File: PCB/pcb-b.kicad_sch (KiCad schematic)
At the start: 23 parts, among them Q13 TPCA8120,L1Q, Q9 BC817, U1 L7805, U2 L7805, U3 L7805

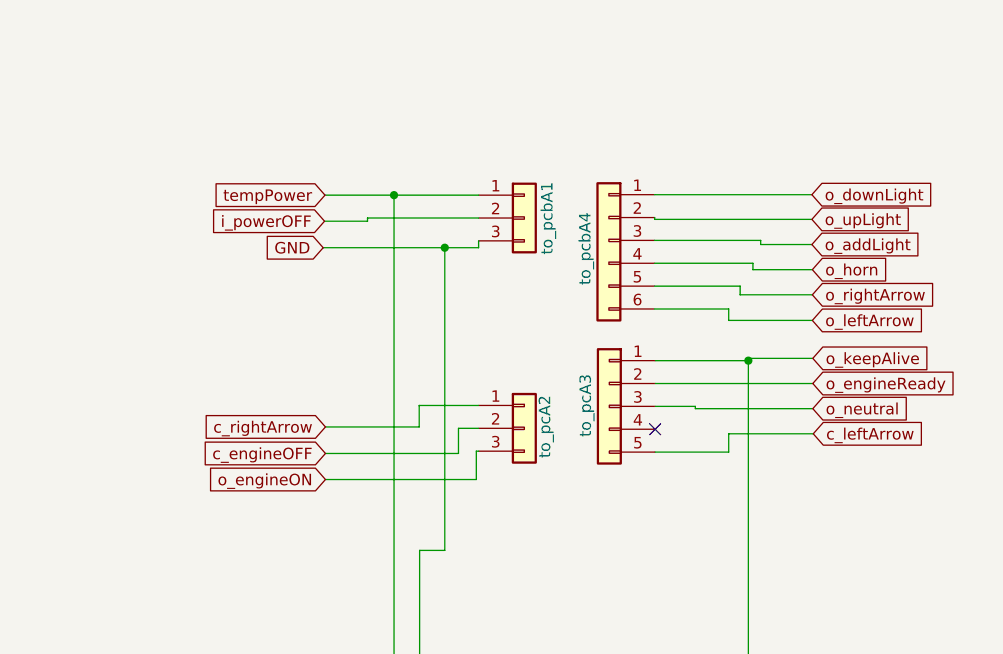
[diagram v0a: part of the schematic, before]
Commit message: Pin-header connectors adjustment
The main idea to mount the two pcb-A on the pcbB has been dropped, because the result is a too much chatic one and I realized that
wires welder on the top is a dangerous solution, they can create unwanted contacts and short-circuits... So, I choise to place the
two PCB beside. So, in order to get a more ordered and clean solution, I am using flat cables instead wires, and pin-header
connectors instead of welding them directly. I foung good connectors where every female-plug is blocked in its male-socket. But,
they are available just for even numbers of pins. For this reason, I have adjusted all the pin-header connectors and their
positions.
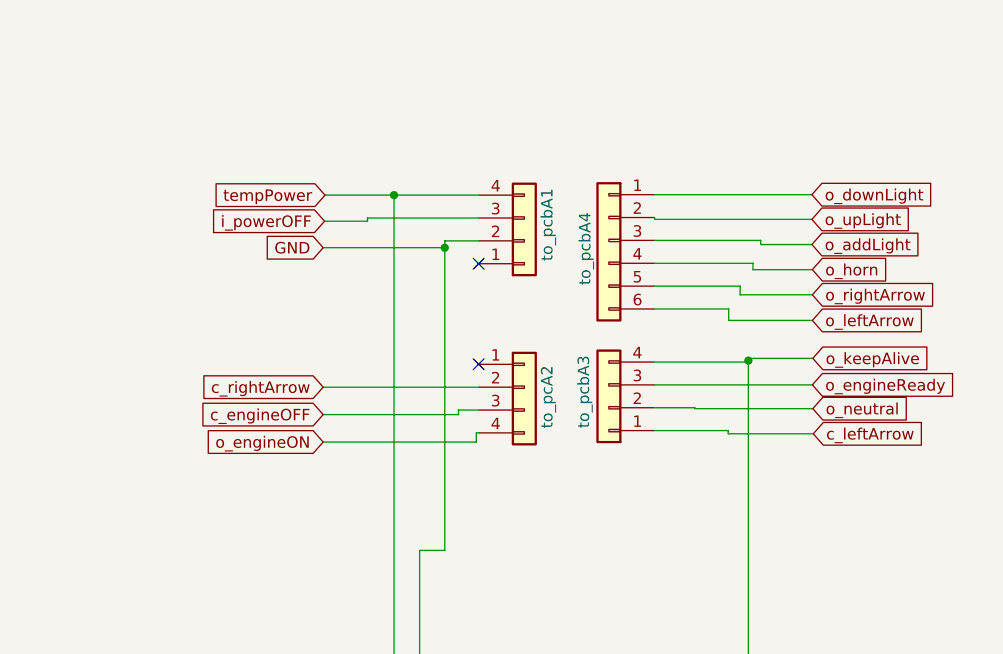
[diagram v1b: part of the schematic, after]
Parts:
- removed to_pcA2, to_pcbA1: Conn_01x03, Connector_PinSocket_2.54mm:PinSocket_1x03_P2.54mm_Vertical, symbol Connector_Generic:Conn_01x03
- removed to_pcA3: Conn_01x05, Connector_PinSocket_2.54mm:PinSocket_1x05_P2.54mm_Vertical, symbol Connector_Generic:Conn_01x05
- added to_pcA2, to_pcbA1, to_pcbA3: Conn_01x04, Connector_PinSocket_2.54mm:PinSocket_1x04_P2.54mm_Vertical, symbol Connector_Generic:Conn_01x04
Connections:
- net GND: now also to_pcbA1.2 (Pin_2)
- net c_engineOFF: now also to_pcA2.3 (Pin_3)
- net c_leftArrow: now also to_pcbA3.1 (Pin_1)
- net c_rightArrow: now also to_pcA2.2 (Pin_2)
- net i_powerOFF: now also to_pcbA1.3 (Pin_3)
- net o_engineON: now also to_pcA2.4 (Pin_4)
- net o_engineReady: now also to_pcbA3.3 (Pin_3)
- net o_keepAlive: now also to_pcbA3.4 (Pin_4)
- net o_neutral: now also to_pcbA3.2 (Pin_2)
- net tempPower: now also to_pcbA1.4 (Pin_4)
- no-connect marks 1 -> 2

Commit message: Important fixes and adjustments
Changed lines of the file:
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@@
-	)
-	(symbol
-		(lib_id "power:PWR_FLAG")
-		(at 140.97 159.512 180)
-		(unit 1)
-		(exclude_from_sim no)
-		(in_bom yes)
-		(on_board yes)
-		(dnp no)
-		(property "Reference" "#FLG0101"
-			(at 140.97 161.417 0)
-			(effects
-				(font
-					(size 1.27 1.27)
-				)
-				(hide yes)
-			)
-		)
-		(property "Value" "PWR_FLAG"
-			(at 140.97 163.576 0)
-			(effects
-				(font
-					(size 1.27 1.27)
-				)
-			)
-		)
-		(property "Footprint" ""
-			(at 140.97 159.512 0)
-			(effects
-				(font
-					(size 1.27 1.27)
-				)
-				(hide yes)
-			)
-		)
-		(property "Datasheet" "~"
-			(at 140.97 159.512 0)
-			(effects
-				(font
-					(size 1.27 1.27)
-				)
-				(hide yes)
-			)
-		)
-		(property "Description" ""
-			(at 140.97 159.512 0)
-			(effects
-				(font
-					(size 1.27 1.27)
-				)
-				(hide yes)
-			)
-		)
-		(pin "1"
-		)
-		(instances
-			(project "pcb-b"
-				(path "/709d0967-afe5-49d3-92a5-d2bb94550bdb"
-					(reference "#FLG0101")
-					(unit 1)
-				)
-			)
-		)
 	)
 	(symbol

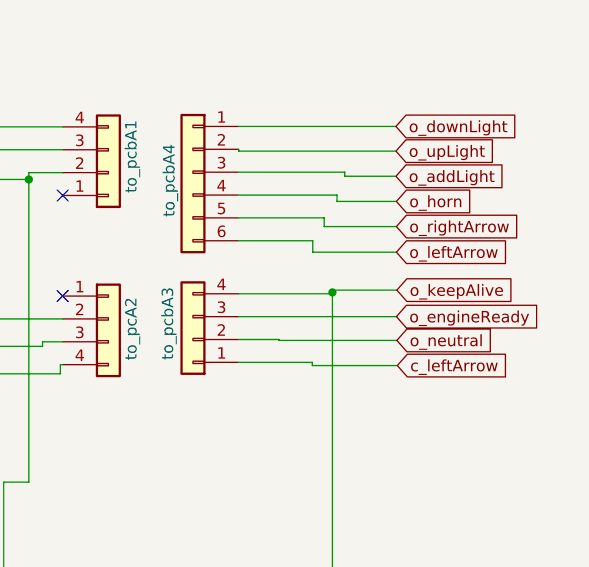
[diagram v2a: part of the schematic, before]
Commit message: o_NEUTRAL is connected directly to the led
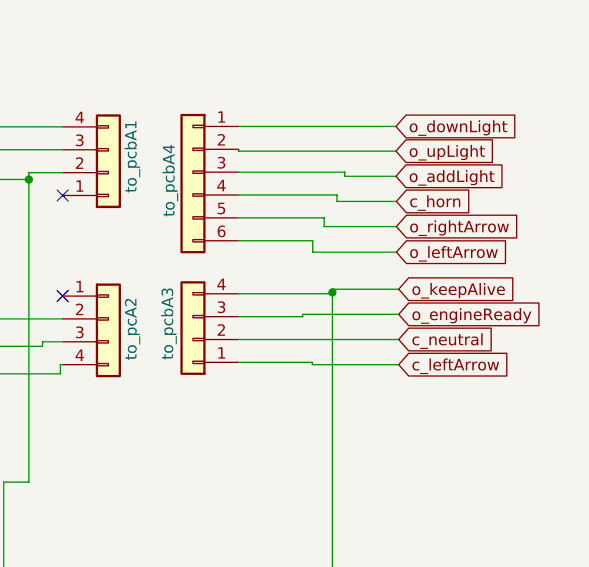
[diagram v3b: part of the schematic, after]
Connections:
- net o_horn renamed c_horn
- net o_neutral renamed c_neutral
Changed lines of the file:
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@@
 	(wire
 		(pts
-			(xy 174.3964 103.124) (xy 169.926 103.124)
-		)
-		(stroke
-			(width 0)
-			(type default)
-		)
-	)
-	(wire
-		(pts
-			(xy 187.5536 106.0196) (xy 178.1048 106.0196)
+			(xy 169.926 103.124) (xy 187.706 103.124)
+		)
+		(stroke
+			(width 0)
+			(type default)
+		)
+	)
+	(wire
+		(pts
+			(xy 177.038 100.33) (xy 187.706 100.33)
+		)
+		(stroke
+			(width 0)
+			(type default)
+		)
+	)
+	(wire
+		(pts
+			(xy 187.706 105.918) (xy 178.1048 105.918)
 		)
 		(stroke
@@
 	(wire
 		(pts
-			(xy 178.1048 106.0196) (xy 178.1048 105.664)
+			(xy 178.1048 105.918) (xy 178.1048 105.664)
 		)
 		(stroke
@@
 	(wire
 		(pts
-			(xy 187.5028 103.2256) (xy 174.3964 103.2256)
-		)
-		(stroke
-			(width 0)
-			(type default)
-		)
-	)
-	(wire
-		(pts
 			(xy 45.72 169.3164) (xy 45.72 171.8564)
 		)
@@
 	(wire
 		(pts
-			(xy 180.34 97.6376) (xy 187.5028 97.6376)
+			(xy 180.34 97.536) (xy 187.706 97.536)
 		)
 		(stroke
@@
 	(wire
 		(pts
+			(xy 177.038 100.584) (xy 169.926 100.584)
+		)
+		(stroke
+			(width 0)
+			(type default)
+		)
+	)
+	(wire
+		(pts
 			(xy 64.9732 114.554) (xy 55.2196 114.554)
 		)
@@
 	(wire
 		(pts
-			(xy 169.926 100.584) (xy 187.5028 100.584)
-		)
-		(stroke
-			(width 0)
-			(type default)
-		)
-	)
-	(wire
-		(pts
 			(xy 135.7122 150.0632) (xy 135.6868 161.544)
 		)
@@
 	(wire
 		(pts
-			(xy 174.3964 103.2256) (xy 174.3964 103.124)
-		)
-		(stroke
-			(width 0)
-			(type default)
-		)
-	)
-	(wire
-		(pts
 			(xy 146.6088 85.344) (xy 146.6088 118.9736)
 		)
@@
 	(wire
 		(pts
+			(xy 177.038 100.33) (xy 177.038 100.584)
+		)
+		(stroke
+			(width 0)
+			(type default)
+		)
+	)
+	(wire
+		(pts
 			(xy 63.4492 158.75) (xy 63.5 158.75)
 		)
@@
 	(wire
 		(pts
-			(xy 180.34 97.8916) (xy 180.34 97.6376)
+			(xy 180.34 97.8916) (xy 180.34 97.536)
 		)
 		(stroke
@@
 		)
 	)
-	(global_label "o_horn"
+	(global_label "c_horn"
 		(shape input)
 		(at 187.452 87.7824 0)
@@
 		)
 		(property "Intersheetrefs" "${INTERSHEET_REFS}"
-			(at 187.452 87.7824 0)
-			(effects
-				(font
-					(size 1.27 1.27)
-				)
+			(at 196.7266 87.7824 0)
+			(effects
+				(font
+					(size 1.27 1.27)
+				)
+				(justify left)
 				(hide yes)
 			)
 		)
 		(property "Riferimenti inter-foglio" "${INTERSHEET_REFS}"
-			(at 196.2151 87.703 0)
+			(at 187.452 89.9732 0)
 			(effects
 				(font
@@
 	(global_label "o_keepAlive"
 		(shape input)
-		(at 187.5028 97.6376 0)
+		(at 187.706 97.536 0)
 		(fields_autoplaced yes)
 		(effects
@@
 		)
 		(property "Intersheetrefs" "${INTERSHEET_REFS}"
-			(at 187.5028 97.6376 0)
+			(at 187.706 97.536 0)
 			(effects
 				(font
@@
 		)
 		(property "Riferimenti inter-foglio" "${INTERSHEET_REFS}"
-			(at 200.8016 97.5582 0)
+			(at 201.0048 97.4566 0)
 			(effects
 				(font
@@
 	(global_label "c_leftArrow"
 		(shape input)
-		(at 187.5536 106.0196 0)
+		(at 187.706 105.918 0)
 		(fields_autoplaced yes)
 		(effects
@@
 		)
 		(property "Intersheetrefs" "${INTERSHEET_REFS}"
-			(at 187.5536 106.0196 0)
+			(at 187.706 105.918 0)
 			(effects
 				(font
@@
 		)
 		(property "Riferimenti inter-foglio" "${INTERSHEET_REFS}"
-			(at 200.3686 105.9402 0)
+			(at 200.521 105.8386 0)
 			(effects
 				(font
@@
 	(global_label "o_engineReady"
 		(shape input)
-		(at 187.452 100.584 0)
+		(at 187.706 100.33 0)
 		(fields_autoplaced yes)
 		(effects
@@
 		)
 		(property "Intersheetrefs" "${INTERSHEET_REFS}"
-			(at 187.452 100.584 0)
+			(at 187.706 100.33 0)
 			(effects
 				(font
@@
 		)
 		(property "Riferimenti inter-foglio" "${INTERSHEET_REFS}"
-			(at 203.8351 100.5046 0)
+			(at 204.0891 100.2506 0)
 			(effects
 				(font
@@
 		)
 	)
-	(global_label "o_neutral"
+	(global_label "c_neutral"
 		(shape input)
-		(at 187.5028 103.2256 0)
+		(at 187.706 103.124 0)
 		(fields_autoplaced yes)
 		(effects
@@
 		)
 		(property "Intersheetrefs" "${INTERSHEET_REFS}"
-			(at 187.5028 103.2256 0)
-			(effects
-				(font
-					(size 1.27 1.27)
-				)
+			(at 199.4601 103.124 0)
+			(effects
+				(font
+					(size 1.27 1.27)
+				)
+				(justify left)
 				(hide yes)
 			)
 		)
 		(property "Riferimenti inter-foglio" "${INTERSHEET_REFS}"
-			(at 198.7454 103.1462 0)
-			(effects
-				(font
+			(at 187.706 105.3148 0)
+			(effects
+				(font

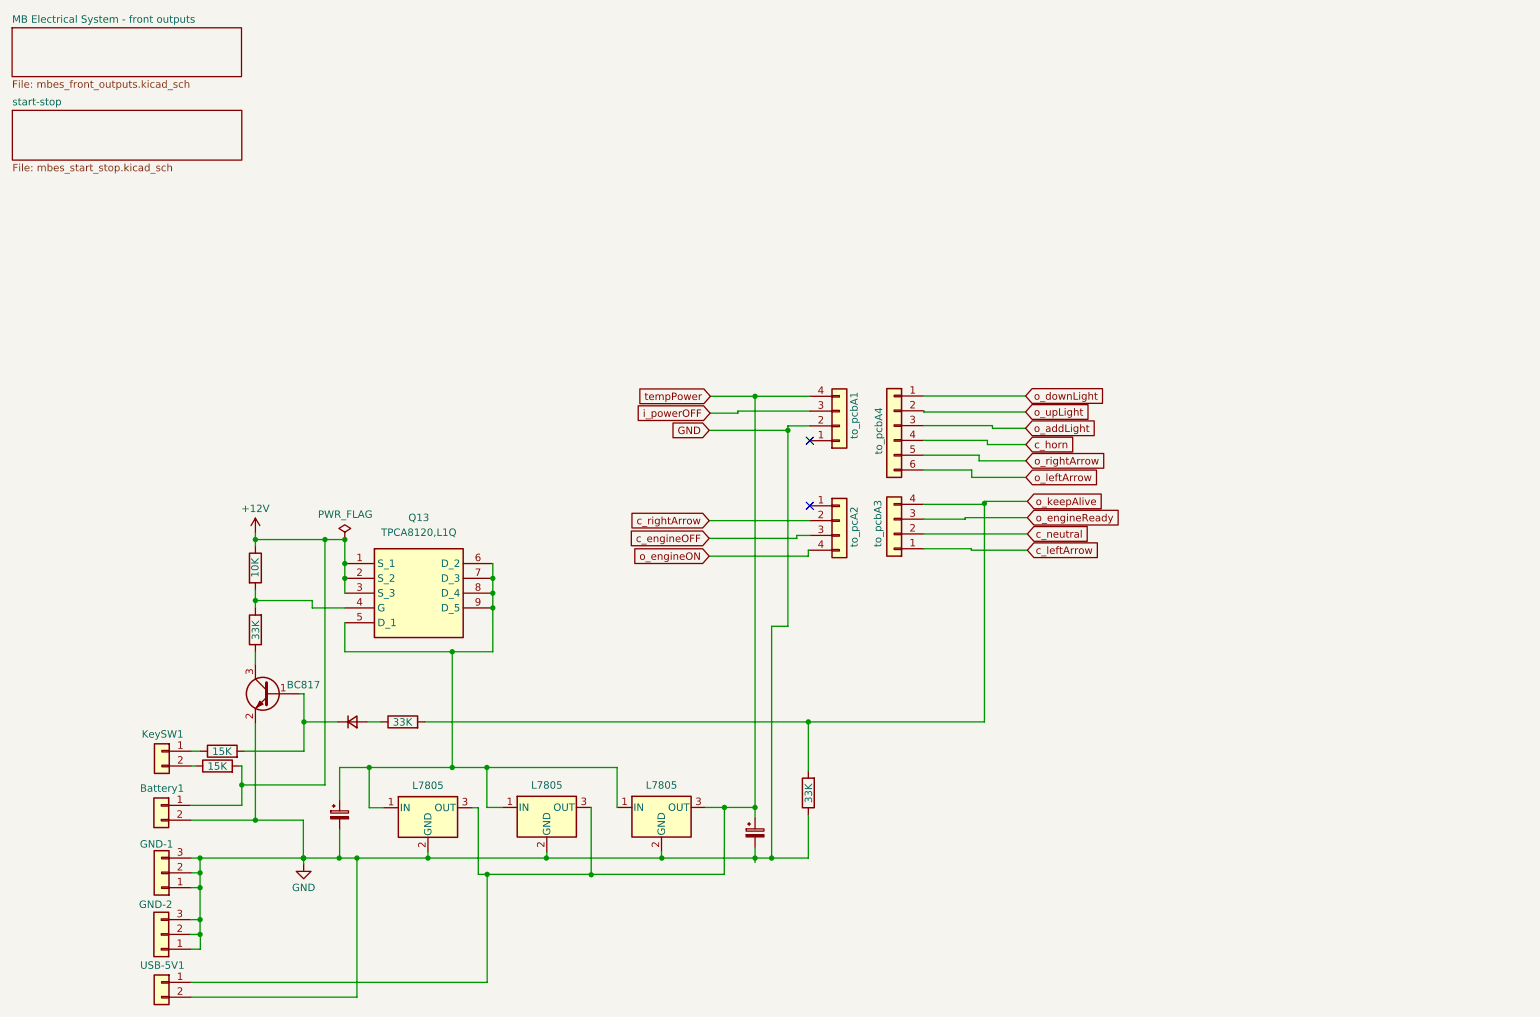
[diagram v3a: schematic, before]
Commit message: No USB support and PCB-B size reducing
Implementing USB power support using 7805 was a stupid idea: too much wasted electic current in Joule effect. So, I moved just
one 7805 in the PCB-A, because the its used power is very low. It allowed me to optimize the PCB-B used space and reduce its
whole size ;-)
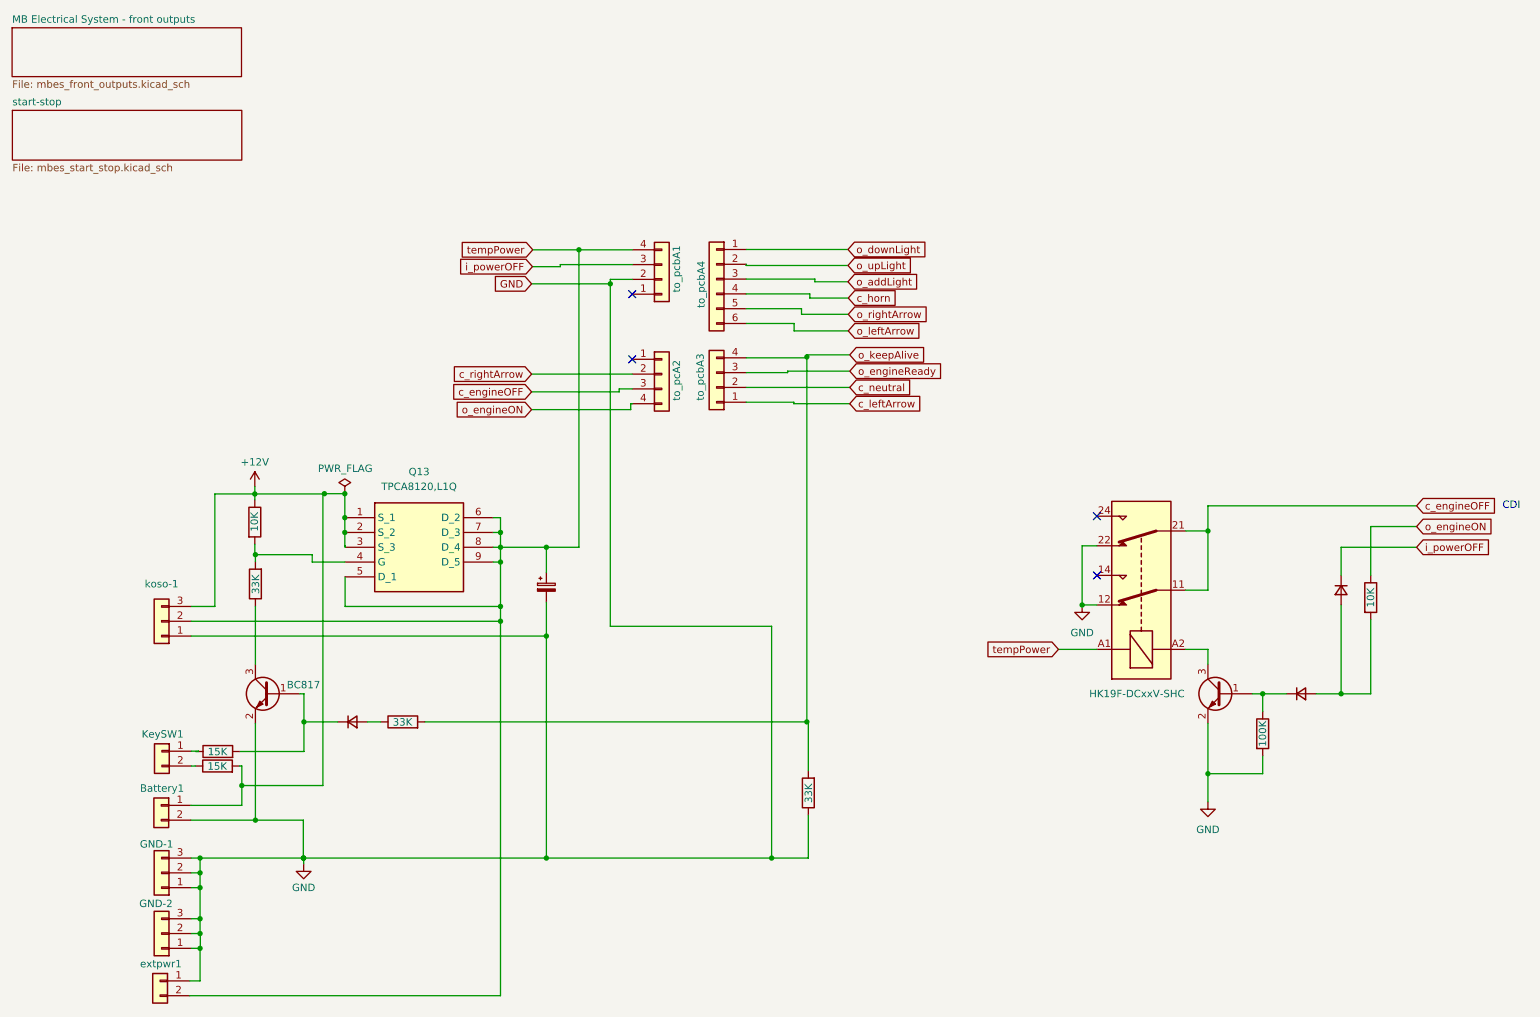
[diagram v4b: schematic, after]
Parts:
- removed C1: C_Polarized_Small, Capacitor_THT:CP_Radial_D8.0mm_P2.50mm, symbol Device:C_Polarized_Small
- removed U1, U2, U3: L7805, Package_TO_SOT_THT:TO-220-3_Vertical, symbol Regulator_Linear:L7805
- removed USB-5V1: Conn_01x02, Connector_Wire:SolderWire-0.75sqmm_1x02_P7mm_D1.25mm_OD3.5mm, symbol Connector_Generic:Conn_01x02
- added D2, D3: D_Small, Diode_SMD:D_1210_3225Metric_Pad1.42x2.65mm_HandSolder, symbol Device:D_Small
- added K1: HK19F-DCxxV-SHC, Relay_THT:Relay_DPDT_Finder_30.22, symbol Relay:HK19F-DCxxV-SHC
- added Q3: BC817, Package_TO_SOT_SMD:SOT-23, symbol Transistor_BJT:BC817
- added RA15: 10K, Resistor_SMD:R_1206_3216Metric, symbol Device:R
- added RA8: 100K, Resistor_SMD:R_1206_3216Metric, symbol Device:R
- added extpwr1: Conn_01x02, Connector_PinHeader_2.54mm:PinHeader_1x02_P2.54mm_Vertical, symbol Connector_Generic:Conn_01x02
- added koso-1: Conn_01x03, Connector_PinHeader_2.54mm:PinHeader_1x03_P2.54mm_Vertical, symbol Connector_Generic:Conn_01x03
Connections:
- net +12V: now also koso-1.3 (Pin_3)
- net GND: now also K1.12, K1.22, Q3.2 (E), RA8.2, extpwr1.1 (Pin_1), koso-1.1 (Pin_1)
- net c_engineOFF: now also K1.11, K1.21
- net i_powerOFF: now also D3.1 (K)
- net o_engineON: now also RA15.1
- net tempPower: now also C9.1, Q13.5 (D_1), Q13.6 (D_2), Q13.7 (D_3), Q13.8 (D_4), Q13.9 (D_5), K1.A1, extpwr1.2 (Pin_2), koso-1.2 (Pin_2)
- new net: D2.1 (K), Q3.1 (B), RA8.1
- new net: K1.A2, Q3.3 (C)
- new net: D2.2 (A), D3.2 (A), RA15.2
- no-connect marks 2 -> 4
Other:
- note added: "CDI"
- moved on the sheet: Q13, to_pcA2, to_pcbA1, to_pcbA3, to_pcbA4

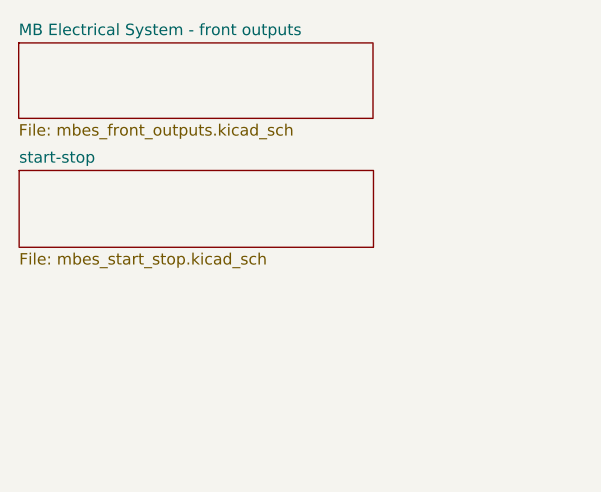
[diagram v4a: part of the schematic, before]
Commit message: PCB size reduction
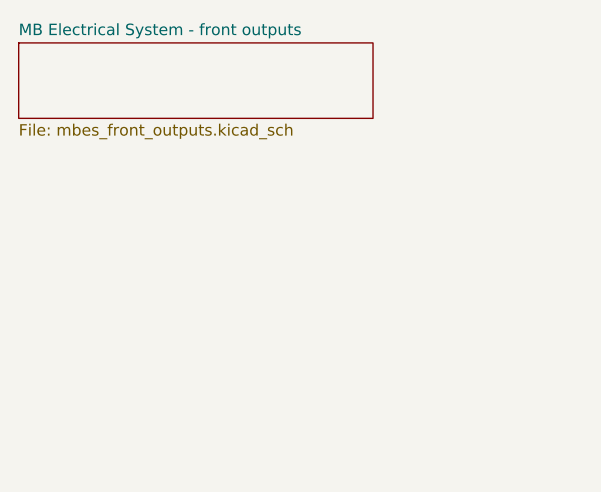
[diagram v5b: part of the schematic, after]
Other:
- removed sheet start-stop
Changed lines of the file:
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@@
-		)
-	)
-	(sheet
-		(at 13.5128 30.4292)
-		(size 39.37 8.5344)
-		(fields_autoplaced yes)
-		(stroke
-			(width 0.1524)
-			(type solid)
-		)
-		(fill
-			(color 0 0 0 0.0000)
-		)
-		(property "Sheetname" "start-stop"
-			(at 13.5128 29.7176 0)
-			(effects
-				(font
-					(size 1.27 1.27)
-				)
-				(justify left bottom)
-			)
-		)
-		(property "Sheetfile" "mbes_start_stop.kicad_sch"
-			(at 13.5128 39.5482 0)
-			(effects
-				(font
-					(size 1.27 1.27)
-				)
-				(justify left top)
-			)
-		)
-		(instances
-			(project "pcb-b"
-				(path "/709d0967-afe5-49d3-92a5-d2bb94550bdb"
-					(page "3")
-				)
-			)
 		)
 	)
